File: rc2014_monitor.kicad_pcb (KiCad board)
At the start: 2 copper layers, 101.6 x 50.8 mm, 60 parts, among them J1 Z80 Bus, J2 Pro Bus, J3 USB_B_Micro, J4 M3 Mounting Hole, SW1 Line Selection, SW2 SW_Push, SW3 SW_Push, SW4 Run/Step Mode, U1 74HCT541, U11 74HCT00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

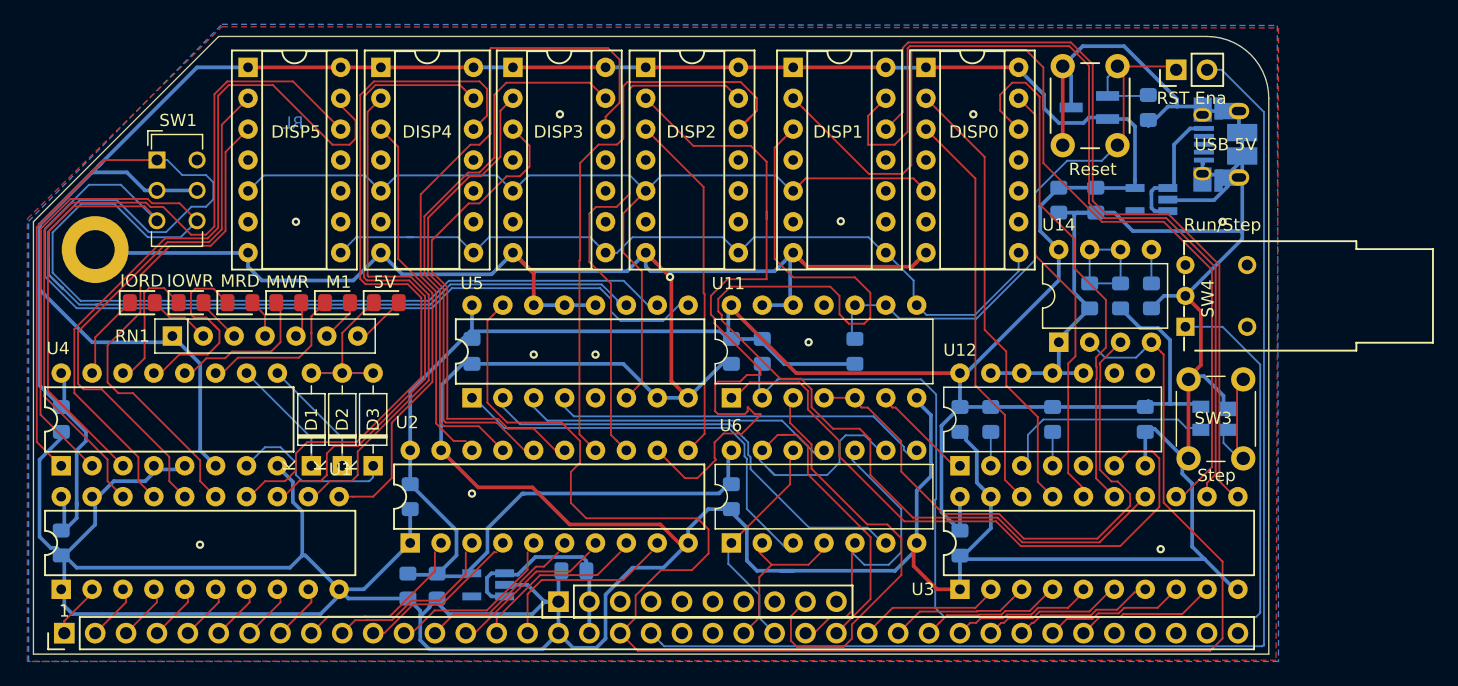
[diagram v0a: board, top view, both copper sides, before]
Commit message: schematic cleanup, improved gnd plane
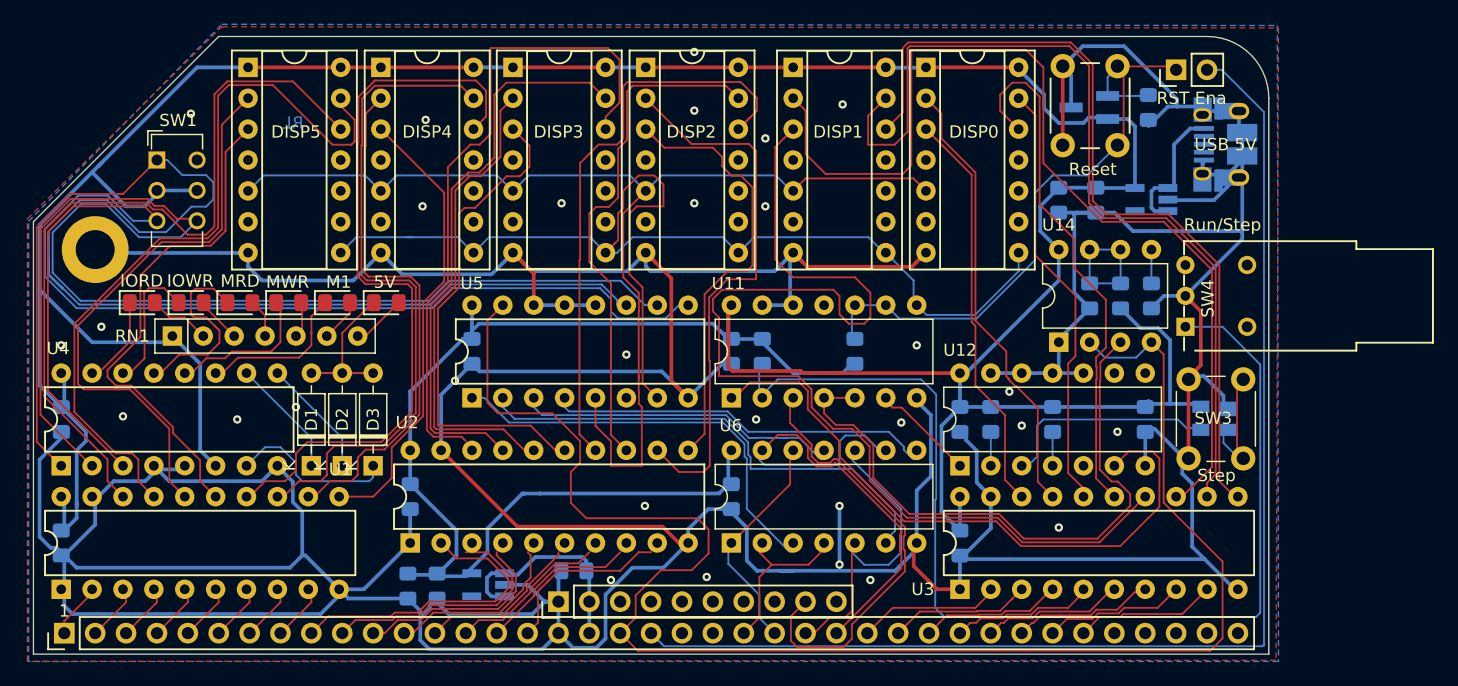
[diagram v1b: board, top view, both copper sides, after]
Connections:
- U5 pad 5: (no net) -> LATCH
- U5 pad 6: LATCH -> (no net)
- U5 pad 7: GND -> RST
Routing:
- net RST: track 66.6 -> 97.3 mm
- net GND: track 543.4 -> 559.0 mm, vias 12 -> 30
- net D_A1: track 59.2 -> 45.1 mm
- net LATCH: track 80.5 -> 94.5 mm
- net A7: track 13.8 -> 25.2 mm
- net D_A0: track 29.0 -> 36.2 mm
- net A6: track 14.0 -> 21.2 mm
- net +5V: track 363.5 -> 369.3 mm
- net A5: track 12.9 -> 17.0 mm
- net D_D4: track 86.3 -> 89.4 mm
- net Net-(U11-Pad4): track 48.3 -> 51.5 mm
- net M_RD: track 38.1 -> 41.1 mm
- net ~IORQ: track 38.7 -> 40.9 mm
- net D_D5: track 79.2 -> 81.3 mm
- net D_A13: track 45.4 -> 47.1 mm
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
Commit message: Swapped out reset, reorganized gnd planes
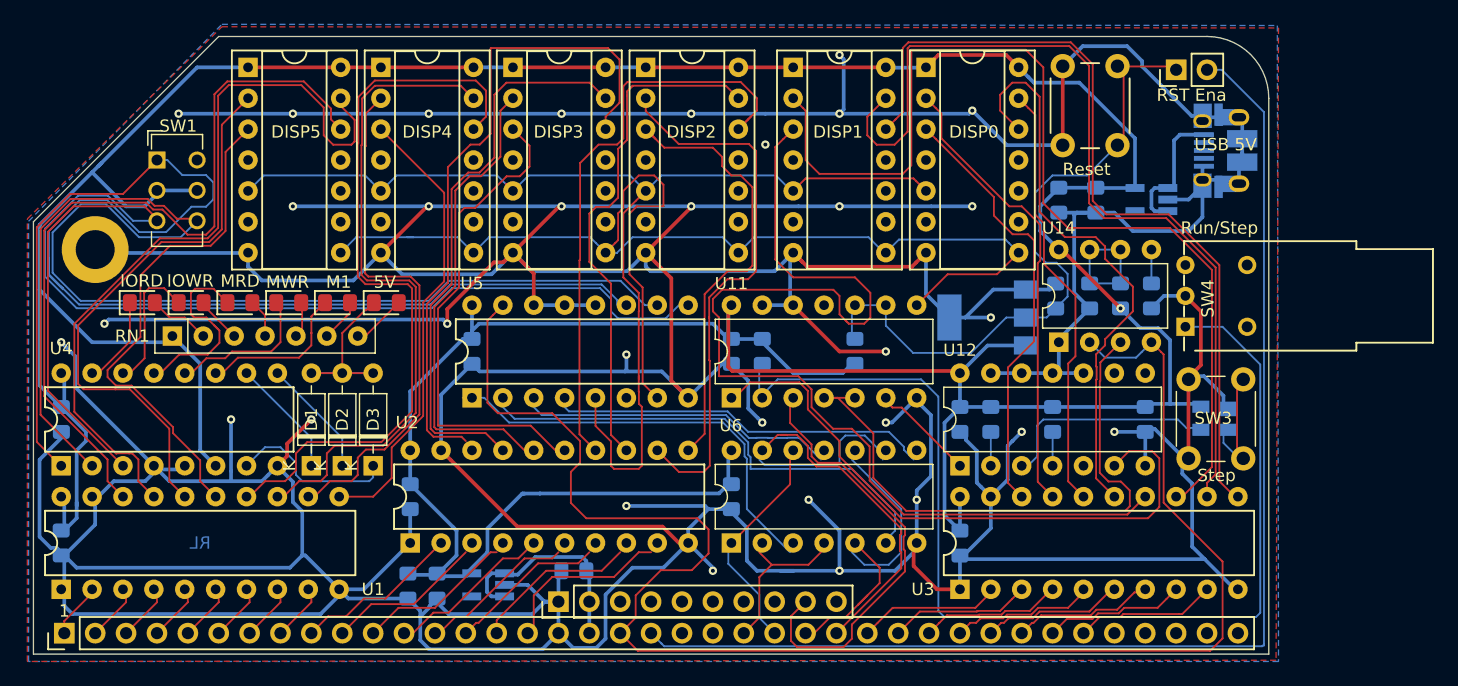
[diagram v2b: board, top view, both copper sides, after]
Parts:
- C9: value 100nF -> 1nF
- U9: value DS1813R-5+T&R -> DS1233Z-5+; footprint Package_TO_SOT_SMD:SOT-23_Handsoldering -> Package_TO_SOT_SMD:SOT-223
- moved U9 19.2 mm to (153.9, 99.8)
- moved C9 17.3 mm to (159.5, 98.1), turned to 90 degrees
- moved J3 0.51 mm to (173.5, 86.1)
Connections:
- U9 pad 1: ~RST -> GND
- U9 pad 2: +5V -> ~RST
- U9 pad 3: GND -> +5V
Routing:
- net GND: track 559.0 -> 808.2 mm, vias 30 -> 32
- net A7: track 25.2 -> 13.7 mm
- net A6: track 21.2 -> 12.9 mm
- net RST: track 97.3 -> 102.3 mm
- net A5: track 17.0 -> 12.9 mm
- net ~RST: track 50.8 -> 54.6 mm
- net D_D3: track 43.7 -> 47.3 mm
- net ~RD: track 23.8 -> 27.2 mm
- net D_D0: track 33.5 -> 36.0 mm
- net D_D5: track 81.3 -> 83.5 mm
- net Net-(U11-Pad1): track 53.7 -> 51.8 mm
- net D_D4: track 89.4 -> 87.5 mm
- net Net-(U11-Pad4): track 51.5 -> 49.7 mm
- net D_A14: track 61.7 -> 63.1 mm
- net A4: track 14.7 -> 13.7 mm
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
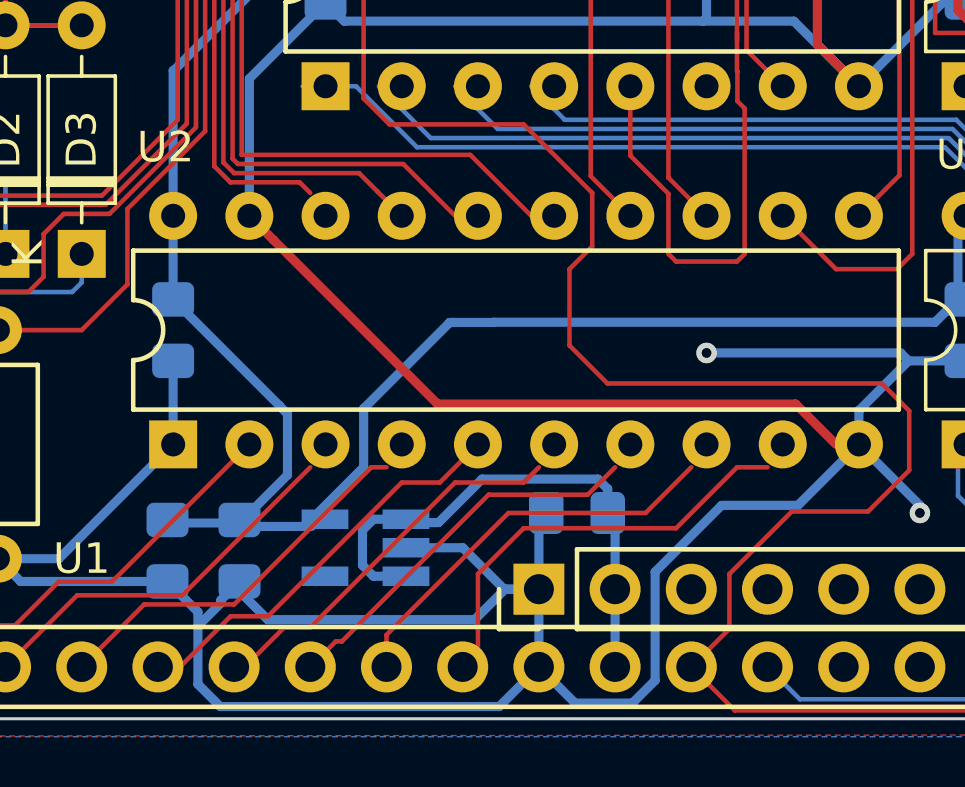
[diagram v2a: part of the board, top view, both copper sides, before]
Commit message: Fixed broken traces
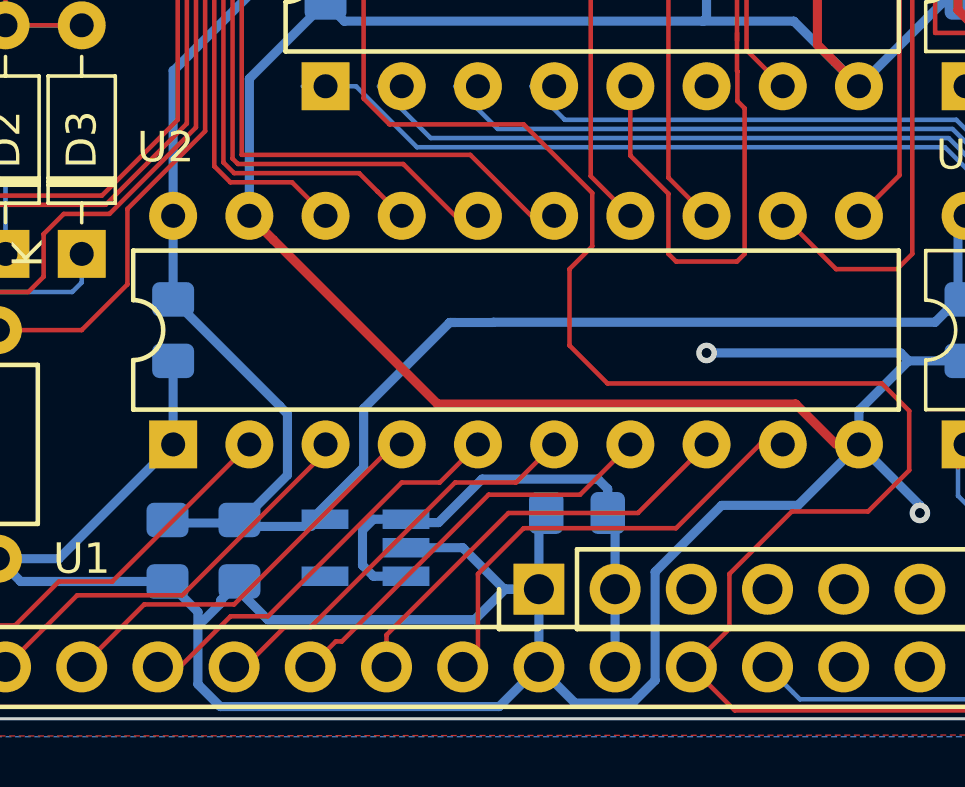
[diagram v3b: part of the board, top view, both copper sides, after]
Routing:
- net A6: track 12.9 -> 13.9 mm
- net A5: track 12.9 -> 13.7 mm
- net A3: track 12.9 -> 13.7 mm
- net A1: track 13.5 -> 14.4 mm
- net D_A7: track 54.8 -> 55.6 mm
- net A0: track 14.4 -> 15.3 mm
- net A2: track 12.9 -> 13.7 mm
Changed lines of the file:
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@@
     (thickness 1.6)
     (drawings 20)
-    (tracks 1380)
+    (tracks 1381)
     (zones 0)
     (modules 60)
@@
     (37 F.SilkS user)
     (38 B.Mask user hide)
-    (39 F.Mask user hide)
+    (39 F.Mask user)
     (44 Edge.Cuts user)
     (45 Margin user hide)
-    (46 B.CrtYd user)
-    (47 F.CrtYd user)
+    (46 B.CrtYd user hide)
+    (47 F.CrtYd user hide)
   )
   (setup
@@
     (aux_axis_origin 0 0)
     (grid_origin 75.438 127.508)
-    (visible_elements FFFFEF7F)
+    (visible_elements FFFFFF7F)
     (pcbplotparams
       (layerselection 0x010f0_ffffffff)
@@
   (segment (start 109.829622 89.256981) (end 109.829622 97.104823) (width 0.1524) (layer F.Cu) (net 48))
   (segment (start 114.338 80.508) (end 113.347622 81.498378) (width 0.1524) (layer F.Cu) (net 48))
-  (segment (start 123.638 82.16633) (end 122.494 83.31033) (width 0.1524) (layer F.Cu) (net 49))
-  (segment (start 122.68941 77.65941) (end 123.638 78.608) (width 0.1524) (layer F.Cu) (net 49))
-  (segment (start 107.797567 109.090768) (end 107.797567 98.705811) (width 0.1524) (layer F.Cu) (net 49))
-  (segment (start 109.524811 96.978567) (end 109.524811 87.452859) (width 0.1524) (layer F.Cu) (net 49))
+  (segment (start 122.494 83.31033) (end 122.494 84.328) (width 0.1524) (layer F.Cu) (net 49))
+  (segment (start 123.638 78.608) (end 123.638 82.16633) (width 0.1524) (layer F.Cu) (net 49))
   (segment (start 113.042811 84.703189) (end 113.042811 77.65941) (width 0.1524) (layer F.Cu) (net 49))
-  (segment (start 113.042811 77.65941) (end 122.68941 77.65941) (width 0.1524) (layer F.Cu) (net 49))
-  (segment (start 109.524811 87.452859) (end 111.37967 85.598) (width 0.1524) (layer F.Cu) (net 49))
-  (segment (start 122.494 83.31033) (end 122.494 84.328) (width 0.1524) (layer F.Cu) (net 49) (status 20))
-  (segment (start 110.642433 109.626433) (end 108.333232 109.626433) (width 0.1524) (layer F.Cu) (net 49))
+  (segment (start 123.638 82.16633) (end 122.494 83.31033) (width 0.1524) (layer F.Cu) (net 49))
+  (segment (start 111.506 110.744) (end 110.388433 109.626433) (width 0.1524) (layer F.Cu) (net 49))
   (segment (start 107.797567 98.705811) (end 109.524811 96.978567) (width 0.1524) (layer F.Cu) (net 49))
-  (segment (start 108.333232 109.626433) (end 107.797567 109.090768) (width 0.1524) (layer F.Cu) (net 49))
+  (segment (start 113.042811 77.65941) (end 122.68941 77.65941) (width 0.1524) (layer F.Cu) (net 49))
+  (segment (start 122.68941 77.65941) (end 123.638 78.608) (width 0.1524) (layer F.Cu) (net 49))
   (segment (start 112.148 85.598) (end 113.042811 84.703189) (width 0.1524) (layer F.Cu) (net 49))
-  (segment (start 123.638 78.608) (end 123.638 82.16633) (width 0.1524) (layer F.Cu) (net 49))
-  (segment (start 110.998 109.982) (end 110.642433 109.626433) (width 0.1524) (layer F.Cu) (net 49) (status 10))
+  (segment (start 109.524811 87.452859) (end 111.37967 85.598) (width 0.1524) (layer F.Cu) (net 49))
   (segment (start 111.37967 85.598) (end 112.148 85.598) (width 0.1524) (layer F.Cu) (net 49))
+  (segment (start 108.333232 109.626433) (end 107.797567 109.090768) (width 0.1524) (layer F.Cu) (net 49))
+  (segment (start 109.524811 96.978567) (end 109.524811 87.452859) (width 0.1524) (layer F.Cu) (net 49))
+  (segment (start 110.388433 109.626433) (end 108.333232 109.626433) (width 0.1524) (layer F.Cu) (net 49))
+  (segment (start 107.797567 109.090768) (end 107.797567 98.705811) (width 0.1524) (layer F.Cu) (net 49))
   (segment (start 116.332 108.712) (end 118.364 110.744) (width 0.1524) (layer F.Cu) (net 50) (status 20))
   (segment (start 114.35433 88.208) (end 111.759562 90.802768) (width 0.1524) (layer F.Cu) (net 50))
@@
   (segment (start 99.681412 124.397388) (end 101.154612 124.397388) (width 0.1524) (layer F.Cu) (net 52))
   (segment (start 98.298 125.7808) (end 99.681412 124.397388) (width 0.1524) (layer F.Cu) (net 52) (status 10))
-  (segment (start 106.730811 123.393189) (end 110.998 119.126) (width 0.1524) (layer F.Cu) (net 53) (status 20))
+  (segment (start 111.506 118.618) (end 111.506 118.364) (width 0.1524) (layer F.Cu) (net 53))
+  (segment (start 106.730811 123.393189) (end 111.506 118.618) (width 0.1524) (layer F.Cu) (net 53))
   (segment (start 103.225611 123.393189) (end 106.730811 123.393189) (width 0.1524) (layer F.Cu) (net 53))
-  (segment (start 100.838 125.7808) (end 103.225611 123.393189) (width 0.1524) (layer F.Cu) (net 53) (status 10))
+  (segment (start 100.838 125.7808) (end 103.225611 123.393189) (width 0.1524) (layer F.Cu) (net 53))
   (segment (start 108.458 123.698) (end 105.4608 123.698) (width 0.1524) (layer F.Cu) (net 54))
-  (segment (start 113.03 119.126) (end 108.458 123.698) (width 0.1524) (layer F.Cu) (net 54))
-  (segment (start 105.4608 123.698) (end 103.378 125.7808) (width 0.1524) (layer F.Cu) (net 54) (status 20))
-  (segment (start 113.538 119.126) (end 113.03 119.126) (width 0.1524) (layer F.Cu) (net 54) (status 10))
+  (segment (start 105.4608 123.698) (end 103.378 125.7808) (width 0.1524) (layer F.Cu) (net 54))
+  (segment (start 113.792 118.364) (end 108.458 123.698) (width 0.1524) (layer F.Cu) (net 54))
+  (segment (start 114.046 118.364) (end 113.792 118.364) (width 0.1524) (layer F.Cu) (net 54))
   (segment (start 115.316 119.634) (end 116.586 118.364) (width 0.1524) (layer F.Cu) (net 55) (status 20))
   (segment (start 114.046 119.634) (end 115.316 119.634) (width 0.1524) (layer F.Cu) (net 55))
@@
   (segment (start 106.6524 125.7808) (end 108.340623 124.092577) (width 0.1524) (layer F.Cu) (net 55) (status 10))
   (segment (start 105.918 125.7808) (end 106.6524 125.7808) (width 0.1524) (layer F.Cu) (net 55) (status 30))
-  (segment (start 118.11 119.634) (end 118.618 119.126) (width 0.1524) (layer F.Cu) (net 56) (status 20))
-  (segment (start 115.824 119.634) (end 118.11 119.634) (width 0.1524) (layer F.Cu) (net 56))
+  (segment (start 117.856 119.634) (end 119.126 118.364) (width 0.1524) (layer F.Cu) (net 56))
+  (segment (start 115.824 119.634) (end 117.856 119.634) (width 0.1524) (layer F.Cu) (net 56))
   (segment (start 110.998 124.46) (end 115.824 119.634) (width 0.1524) (layer F.Cu) (net 56))
-  (segment (start 108.8136 125.7808) (end 110.1344 124.46) (width 0.1524) (layer F.Cu) (net 56) (status 10))
   (segment (start 110.1344 124.46) (end 110.998 124.46) (width 0.1524) (layer F.Cu) (net 56))
-  (segment (start 108.458 125.7808) (end 108.8136 125.7808) (width 0.1524) (layer F.Cu) (net 56) (status 30))
-  (segment (start 116.941622 120.040378) (end 120.243622 120.040378) (width 0.1524) (layer F.Cu) (net 57))
+  (segment (start 108.8136 125.7808) (end 110.1344 124.46) (width 0.1524) (layer F.Cu) (net 56))
+  (segment (start 108.458 125.7808) (end 108.8136 125.7808) (width 0.1524) (layer F.Cu) (net 56))
+  (segment (start 119.989622 120.040378) (end 121.666 118.364) (width 0.1524) (layer F.Cu) (net 57))
   (segment (start 112.051199 124.930801) (end 116.941622 120.040378) (width 0.1524) (layer F.Cu) (net 57))
-  (segment (start 120.243622 120.040378) (end 121.158 119.126) (width 0.1524) (layer F.Cu) (net 57) (status 20))
-  (segment (start 111.847999 124.930801) (end 112.051199 124.930801) (width 0.1524) (layer F.Cu) (net 57) (status 10))
-  (segment (start 110.998 125.7808) (end 111.847999 124.930801) (width 0.1524) (layer F.Cu) (net 57) (status 30))
-  (segment (start 122.174 120.65) (end 123.698 119.126) (width 0.1524) (layer F.Cu) (net 58) (status 20))
-  (segment (start 117.602 120.65) (end 122.174 120.65) (width 0.1524) (layer F.Cu) (net 58))
+  (segment (start 116.941622 120.040378) (end 119.989622 120.040378) (width 0.1524) (layer F.Cu) (net 57))
+  (segment (start 111.847999 124.930801) (end 112.051199 124.930801) (width 0.1524) (layer F.Cu) (net 57))
+  (segment (start 110.998 125.7808) (end 111.847999 124.930801) (width 0.1524) (layer F.Cu) (net 57))
+  (segment (start 121.92 120.65) (end 124.206 118.364) (width 0.1524) (layer F.Cu) (net 58))
+  (segment (start 117.602 120.65) (end 121.92 120.65) (width 0.1524) (layer F.Cu) (net 58))
   (segment (start 113.538 124.714) (end 117.602 120.65) (width 0.1524) (layer F.Cu) (net 58))
-  (segment (start 113.538 125.7808) (end 113.538 124.714) (width 0.1524) (layer F.Cu) (net 58) (status 10))
+  (segment (start 113.538 125.7808) (end 113.538 124.714) (width 0.1524) (layer F.Cu) (net 58))
+  (segment (start 116.586 125.2728) (end 116.078 125.7808) (width 0.1524) (layer F.Cu) (net 59))
+  (segment (start 116.586 122.682) (end 116.586 125.2728) (width 0.1524) (layer F.Cu) (net 59))
+  (segment (start 125.984 118.364) (end 123.19 121.158) (width 0.1524) (layer F.Cu) (net 59))
   (segment (start 118.11 121.158) (end 116.586 122.682) (width 0.1524) (layer F.Cu) (net 59))
-  (segment (start 116.586 122.682) (end 116.586 125.2728) (width 0.1524) (layer F.Cu) (net 59) (status 20))
-  (segment (start 125.222 119.126) (end 123.19 121.158) (width 0.1524) (layer F.Cu) (net 59))
   (segment (start 123.19 121.158) (end 118.11 121.158) (width 0.1524) (layer F.Cu) (net 59))
-  (segment (start 116.586 125.2728) (end 116.078 125.7808) (width 0.1524) (layer F.Cu) (net 59) (status 30))
-  (segment (start 126.238 119.126) (end 125.222 119.126) (width 0.1524) (layer F.Cu) (net 59) (status 10))
+  (segment (start 126.746 118.364) (end 125.984 118.364) (width 0.1524) (layer F.Cu) (net 59))
   (segment (start 144.867999 124.930801) (end 144.018 125.7808) (width 0.1524) (layer F.Cu) (net 60) (status 30))
   (segment (start 154.178 122.428) (end 152.908 123.698) (width 0.1524) (layer F.Cu) (net 60) (status 10))
